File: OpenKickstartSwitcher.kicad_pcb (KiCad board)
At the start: 2 copper layers, 28.1 x 69.1 mm, 9 parts, among them J1 Conn_01x03, J2 Conn_01x03, U1 KS_SOCKET, U2 M27C800, U3 7400

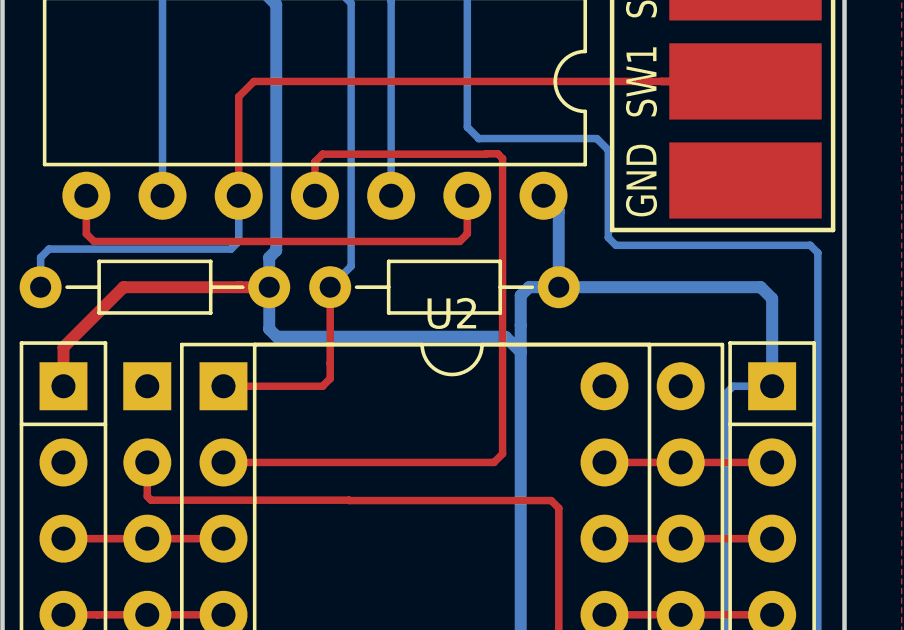
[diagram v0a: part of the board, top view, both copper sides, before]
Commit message: Fix EPROM footprint
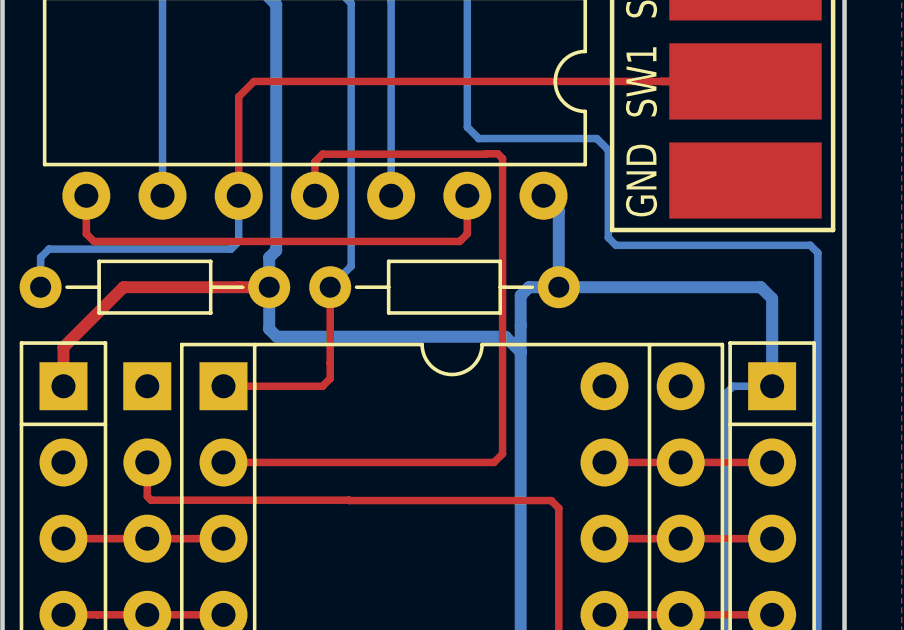
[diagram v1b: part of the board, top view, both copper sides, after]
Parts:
- U2: footprint Housings_DIP:DIP-42_W15.24mm_Socket -> OpenKickstartSwitcher:DIP-42_Socket
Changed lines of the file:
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@@
   (general
     (links 79)
-    (no_connects 6)
+    (no_connects 0)
     (area 143.942999 88.316999 172.160001 157.555001)
     (thickness 1.6)
@@
       (effects (font (size 1 1) (thickness 0.15)))
     )
-    (fp_text value 10k (at 3.81 1.86 180) (layer F.Fab)
+    (fp_text value 10k (at 3.81 0 180) (layer F.Fab)
       (effects (font (size 1 1) (thickness 0.15)))
     )
@@
       (effects (font (size 1 1) (thickness 0.15)))
     )
-    (fp_text value 10k (at 3.81 1.86 180) (layer F.Fab)
+    (fp_text value 10k (at 3.81 0 180) (layer F.Fab)
       (effects (font (size 1 1) (thickness 0.15)))
     )
@@
       (effects (font (size 1 1) (thickness 0.15)))
     )
-    (fp_text value 7400 (at 3.81 17.63 270) (layer F.Fab)
-      (effects (font (size 1 1) (thickness 0.15)))
-    )
-    (fp_text user %R (at 3.81 7.62 270) (layer F.Fab)
+    (fp_text value 7400 (at 3.81 7.62 360) (layer F.Fab)
+      (effects (font (size 1 1) (thickness 0.15)))
+    )
+    (fp_text user %R (at 3.81 7.62 270) (layer F.Fab) hide
       (effects (font (size 1 1) (thickness 0.15)))
     )
@@
       (effects (font (size 1 1) (thickness 0.15)))
     )
-    (fp_text value KS_SOCKET (at 7.62 53.19) (layer F.Fab)
+    (fp_text value KS_SOCKET (at 7.62 53.19) (layer F.Fab) hide
       (effects (font (size 1 1) (thickness 0.15)))
     )
@@
       (effects (font (size 1 1) (thickness 0.15)))
     )
-    (fp_text value Conn_01x03 (at 0 7.47 180) (layer F.Fab)
+    (fp_text value Conn_01x03 (at 0 7.47 180) (layer F.Fab) hide
       (effects (font (size 1 1) (thickness 0.15)))
     )
@@
     )
   )
-  (module Housings_DIP:DIP-42_W15.24mm_Socket (layer F.Cu)
+  (module OpenKickstartSwitcher:DIP-42_Socket (layer F.Cu)
     (at 151.384 104.902)
     (descr "42-lead dip package, row spacing 15.24 mm (600 mils), Socket")
     (tags "DIL DIP PDIP 2.54mm 15.24mm 600mil Socket")
-    (fp_text reference U2 (at 7.62 -2.39) (layer F.SilkS)
+    (fp_text reference U2 (at 7.62 -2.39) (layer F.SilkS) hide
       (effects (font (size 1 1) (thickness 0.15)))
     )
@@
       (effects (font (size 1 1) (thickness 0.15)))
     )
-    (fp_text user %R (at 7.62 25.4) (layer F.Fab)
+    (fp_text user %R (at 7.62 25.4) (layer F.Fab) hide
       (effects (font (size 1 1) (thickness 0.15)))
     )
@@
     (fp_line (start 16.51 52.07) (end 16.51 -1.27) (layer F.Fab) (width 0.1))
     (fp_line (start 16.51 -1.27) (end -1.27 -1.27) (layer F.Fab) (width 0.1))
-    (fp_line (start 6.62 -1.39) (end 1.04 -1.39) (layer F.SilkS) (width 0.12))
+    (fp_line (start 6.62 -1.39) (end -1.39 -1.39) (layer F.SilkS) (width 0.12))
     (fp_line (start 1.04 -1.39) (end 1.04 52.19) (layer F.SilkS) (width 0.12))
     (fp_line (start 1.04 52.19) (end 14.2 52.19) (layer F.SilkS) (width 0.12))
     (fp_line (start 14.2 52.19) (end 14.2 -1.39) (layer F.SilkS) (width 0.12))
-    (fp_line (start 14.2 -1.39) (end 8.62 -1.39) (layer F.SilkS) (width 0.12))
+    (fp_line (start 16.63 -1.39) (end 8.62 -1.39) (layer F.SilkS) (width 0.12))
     (fp_line (start -1.39 -1.39) (end -1.39 52.19) (layer F.SilkS) (width 0.12))
     (fp_line (start -1.39 52.19) (end 16.63 52.19) (layer F.SilkS) (width 0.12))
     (fp_line (start 16.63 52.19) (end 16.63 -1.39) (layer F.SilkS) (width 0.12))
-    (fp_line (start 16.63 -1.39) (end -1.39 -1.39) (layer F.SilkS) (width 0.12))
     (fp_line (start -1.7 -1.7) (end -1.7 52.5) (layer F.CrtYd) (width 0.05))
     (fp_line (start -1.7 52.5) (end 16.9 52.5) (layer F.CrtYd) (width 0.05))
@@
     (effects (font (size 1 0.8) (thickness 0.15)))
   )
-  (dimension 27.686 (width 0.3) (layer F.Fab)
-    (gr_text "27,686 mm" (at 157.861 79.930001) (layer F.Fab)
+  (dimension 28.067 (width 0.3) (layer F.Fab)
+    (gr_text "28,067 mm" (at 158.0515 80.946001) (layer F.Fab)
       (effects (font (size 1.5 1.5) (thickness 0.3)))
     )
-    (feature1 (pts (xy 144.018 87.376) (xy 144.018 78.580001)))
-    (feature2 (pts (xy 171.704 87.376) (xy 171.704 78.580001)))
-    (crossbar (pts (xy 171.704 81.280001) (xy 144.018 81.280001)))
-    (arrow1a (pts (xy 144.018 81.280001) (xy 145.144504 80.69358)))
-    (arrow1b (pts (xy 144.018 81.280001) (xy 145.144504 81.866422)))
-    (arrow2a (pts (xy 171.704 81.280001) (xy 170.577496 80.69358)))
-    (arrow2b (pts (xy 171.704 81.280001) (xy 170.577496 81.866422)))
-  )
-  (dimension 70.104 (width 0.3) (layer F.Fab)
-    (gr_text "70,104 mm" (at 180.42 122.428 270) (layer F.Fab)
+    (feature1 (pts (xy 144.018 88.392) (xy 144.018 79.596001)))
+    (feature2 (pts (xy 172.085 88.392) (xy 172.085 79.596001)))
+    (crossbar (pts (xy 172.085 82.296001) (xy 144.018 82.296001)))
+    (arrow1a (pts (xy 144.018 82.296001) (xy 145.144504 81.70958)))
+    (arrow1b (pts (xy 144.018 82.296001) (xy 145.144504 82.882422)))
+    (arrow2a (pts (xy 172.085 82.296001) (xy 170.958496 81.70958)))
+    (arrow2b (pts (xy 172.085 82.296001) (xy 170.958496 82.882422)))
+  )
+  (dimension 69.088 (width 0.3) (layer F.Fab)
+    (gr_text "69,088 mm" (at 180.801 122.936 270) (layer F.Fab)
       (effects (font (size 1.5 1.5) (thickness 0.3)))
     )
-    (feature1 (pts (xy 171.704 157.48) (xy 181.77 157.48)))
-    (feature2 (pts (xy 171.704 87.376) (xy 181.77 87.376)))
-    (crossbar (pts (xy 179.07 87.376) (xy 179.07 157.48)))
-    (arrow1a (pts (xy 179.07 157.48) (xy 178.483579 156.353496)))
-    (arrow1b (pts (xy 179.07 157.48) (xy 179.656421 156.353496)))
-    (arrow2a (pts (xy 179.07 87.376) (xy 178.483579 88.502504)))
-    (arrow2b (pts (xy 179.07 87.376) (xy 179.656421 88.502504)))
+    (feature1 (pts (xy 172.085 157.48) (xy 182.151 157.48)))
+    (feature2 (pts (xy 172.085 88.392) (xy 182.151 88.392)))
+    (crossbar (pts (xy 179.451 88.392) (xy 179.451 157.48)))
+    (arrow1a (pts (xy 179.451 157.48) (xy 178.864579 156.353496)))
+    (arrow1b (pts (xy 179.451 157.48) (xy 180.037421 156.353496)))
+    (arrow2a (pts (xy 179.451 88.392) (xy 178.864579 89.518504)))
+    (arrow2b (pts (xy 179.451 88.392) (xy 180.037421 89.518504)))
   )
   (gr_line (start 170.815 88.392) (end 145.288 88.392) (layer Edge.Cuts) (width 0.15))

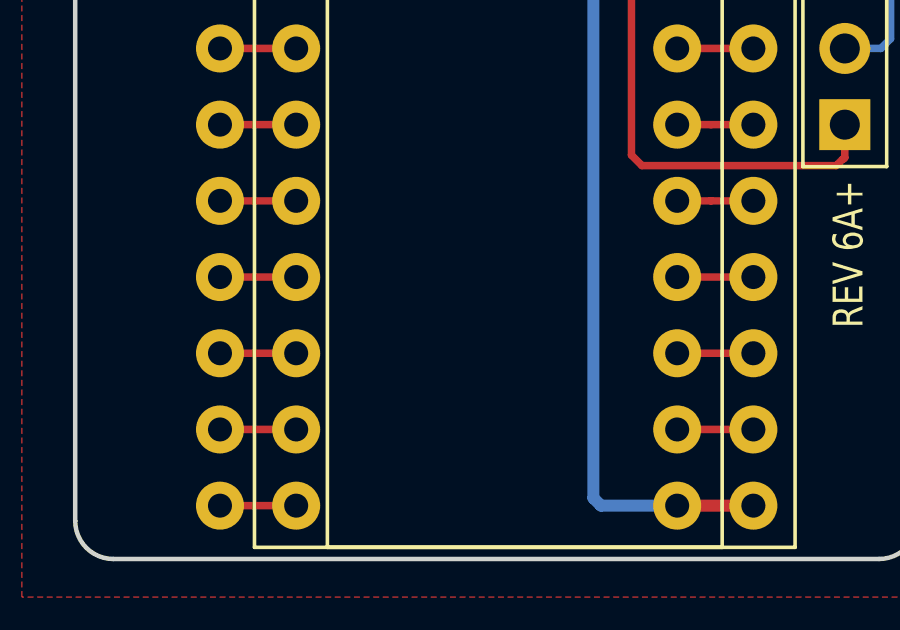
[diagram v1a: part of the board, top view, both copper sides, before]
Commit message: Add OSHW logo and URL
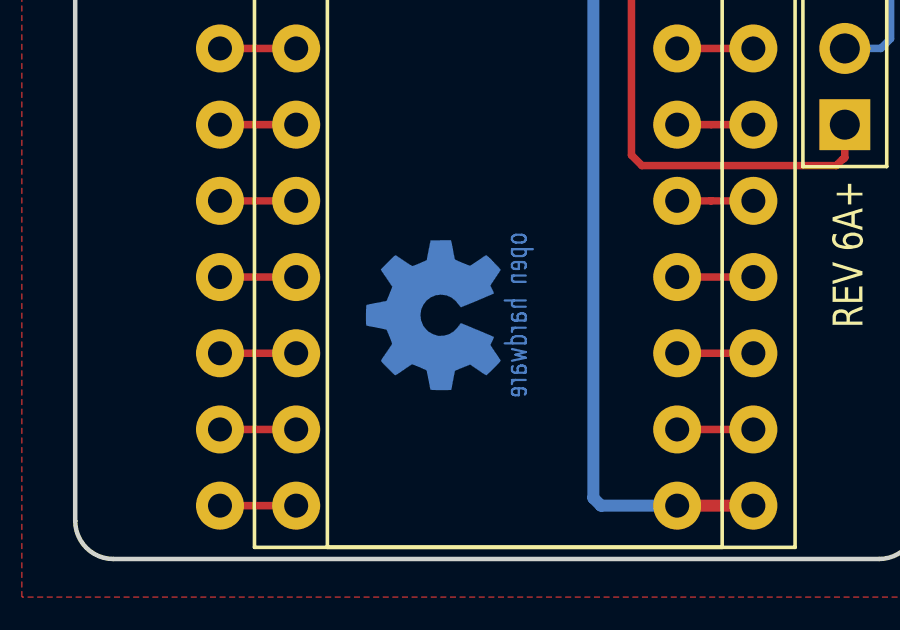
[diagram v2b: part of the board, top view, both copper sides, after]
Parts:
- added J99: OSHW_LOGO, w_logo:Logo_copper_OSHW_6x6mm, B.Cu at (156.0, 149.4)
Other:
- board text added: "github.com/SukkoPera/OpenKickstartSwitcher"

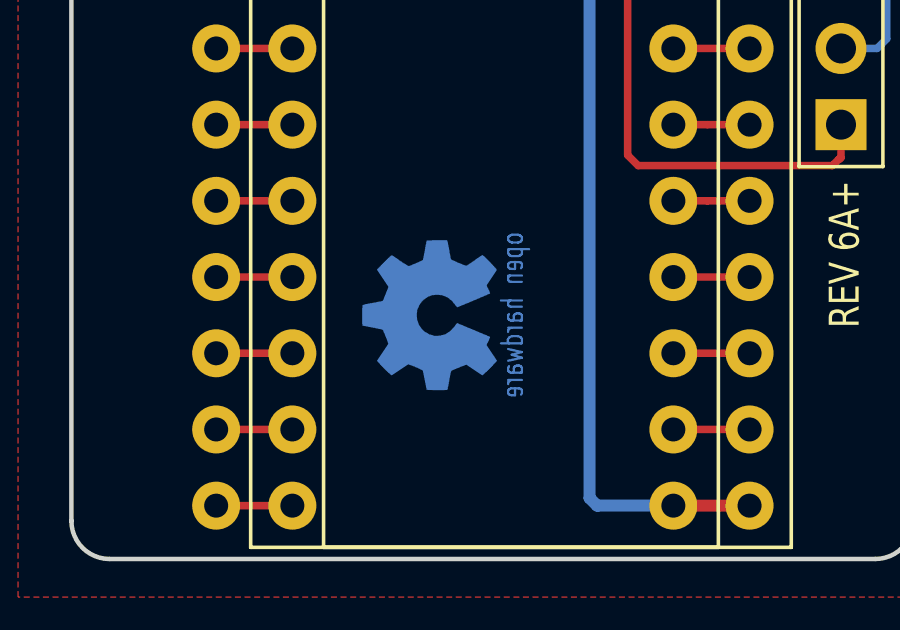
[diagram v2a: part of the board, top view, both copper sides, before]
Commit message: Move logo/URL slightly
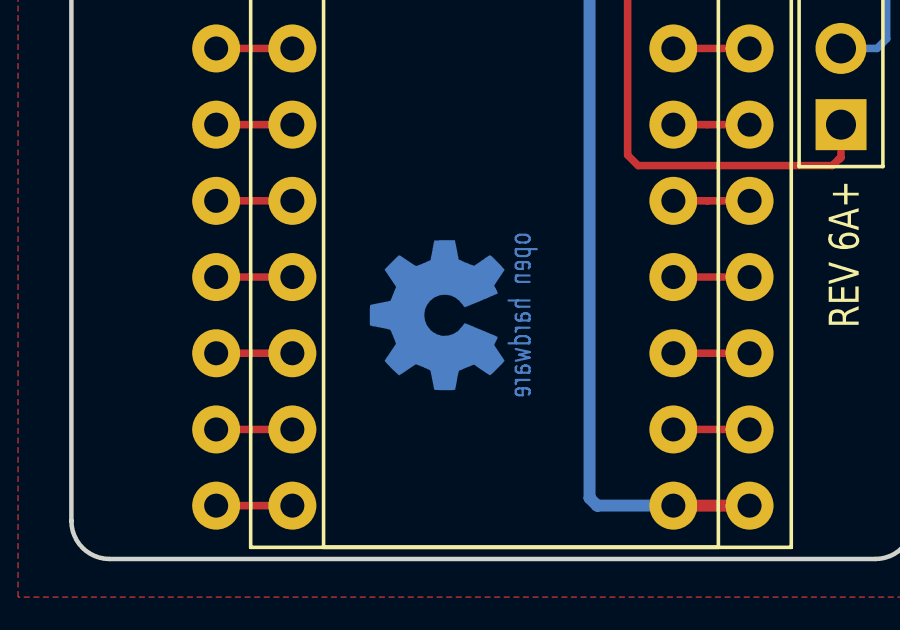
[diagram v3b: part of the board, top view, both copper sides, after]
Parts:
- moved J99 0.25 mm to (156.2, 149.4)
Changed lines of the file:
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@@
   )
   (module w_logo:Logo_copper_OSHW_6x6mm (layer B.Cu)
-    (at 155.956 149.352 270)
+    (at 156.21 149.352 270)
     (descr "Open Hardware Logo, 6x6mm")
     (fp_text reference J99 (at 0 0 270) (layer B.SilkS) hide
@@
       (xy -1.51384 -2.24536)) (layer B.Cu) (width 0.00254))
   )
-  (gr_text github.com/SukkoPera/OpenKickstartSwitcher (at 156.464 125.603 90) (layer B.SilkS)
+  (gr_text github.com/SukkoPera/OpenKickstartSwitcher (at 156.718 125.603 90) (layer B.SilkS)
     (effects (font (size 1 1) (thickness 0.15)) (justify mirror))
   )
